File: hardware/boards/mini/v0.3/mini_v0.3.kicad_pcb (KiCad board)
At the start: 8 copper layers, 20 x 40 mm, 94 parts, among them IC1 NAU88C22YG, IC3 IS42S16160J-6BLI, J4 DF40C-90DP-0.4V, U2 LTV-217-G, U3 W25Q128JVS, U4 STM32H750XBHx, Y1 Crystal_GND24, Y3 32.768kHz

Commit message: mini: various final DFM tweaks
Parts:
- added G***: LOGO, LOGO, B.Cu at (72.4, 84.0)
- added kibuzzard-69637FF5: G***, kibuzzard-69637FF5, F.Cu at (71.5, 67.0)
- added kibuzzard-696388A5: G***, kibuzzard-696388A5, F.Cu at (88.5, 71.8)
- moved D2 4.51 mm to (85.0, 58.3)
- moved R15 4.51 mm to (82.8, 58.1)
- moved D3 0.15 mm to (79.6, 87.2)
- moved FB2 0.15 mm to (78.2, 88.2)
- moved FB3 0.15 mm to (81.5, 88.4)
- moved R6 0.15 mm to (88.5, 85.0)
- moved R7 0.15 mm to (78.2, 86.3)
- moved U2 0.15 mm to (85.0, 86.7)
- moved D4 0.13 mm to (75.5, 58.3)
- moved R17 0.07 mm to (73.5, 58.1)
- moved C26 0.06 mm to (84.5, 95.1)
- moved C27 0.06 mm to (83.6, 95.1)
- moved C20 0.05 mm to (86.3, 95.1)
- moved C21 0.05 mm to (85.4, 95.1)
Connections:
- U4 pad A12: unconnected-(U4D-PD4-PadA12) -> /LED_STATUS
- U4 pad A4: unconnected-(U4I-PI4-PadA4) -> /LED_STATUS2
- U4 pad E3: /LED_STATUS -> unconnected-(U4C-PC13-PadE3)
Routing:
- net /LED_STATUS2: track 0.00 -> 3.74 mm
- net +3.3V: track 54.9 -> 57.1 mm
- net /LED_STATUS: track 0.00 -> 2.22 mm
- net /SPKL: track 17.6 -> 19.6 mm, vias 1 -> 2
- net /SPKR: track 15.9 -> 16.1 mm, vias 1 -> 2
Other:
- outline, holes or cut-outs redrawn
- board text added: "Corners bites radius is 1.1mm for M2 mounting bolts."
- board text added: "DF40C-90DP-0.4V"
- board text added: "QSPI FLASH"
- board text added: "SDRAM"
- board text added: "White square is replaced with a 5x5mm QR code by JLC when configured in the order."

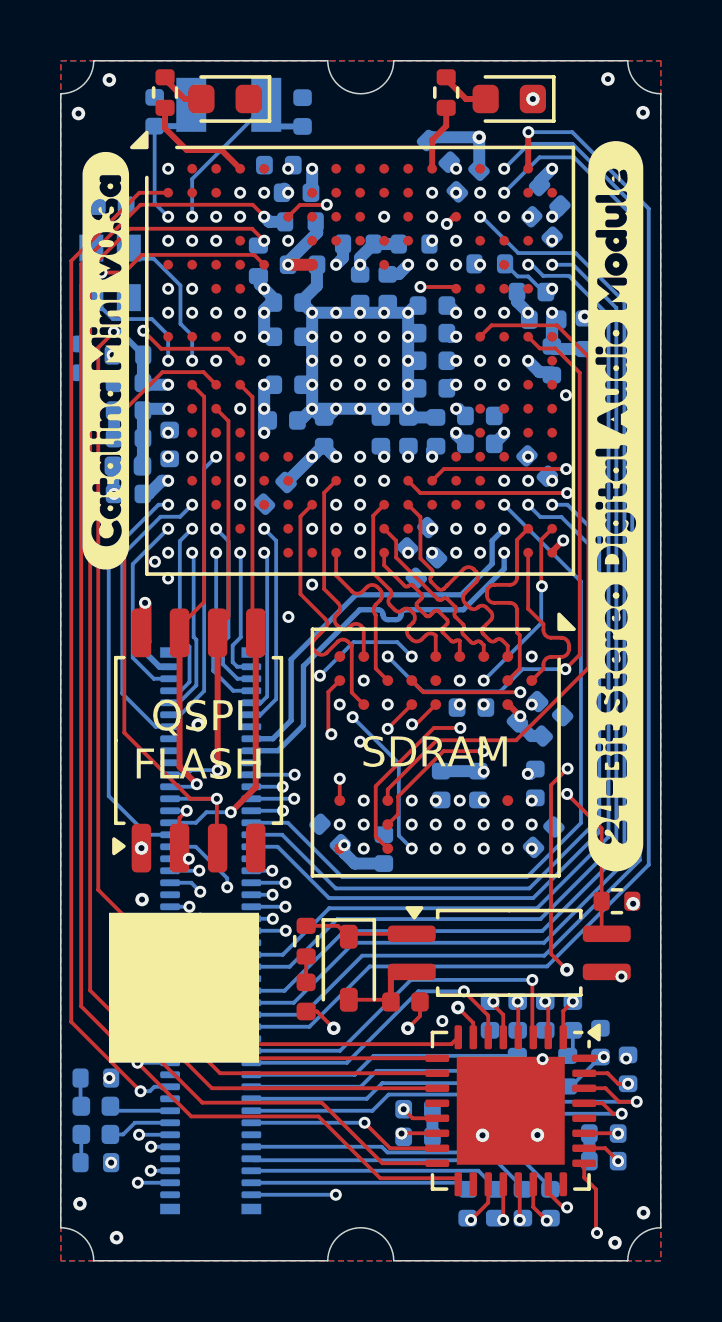
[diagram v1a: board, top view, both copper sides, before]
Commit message: mini: re-route status LED, add paws, expose copper on screw points
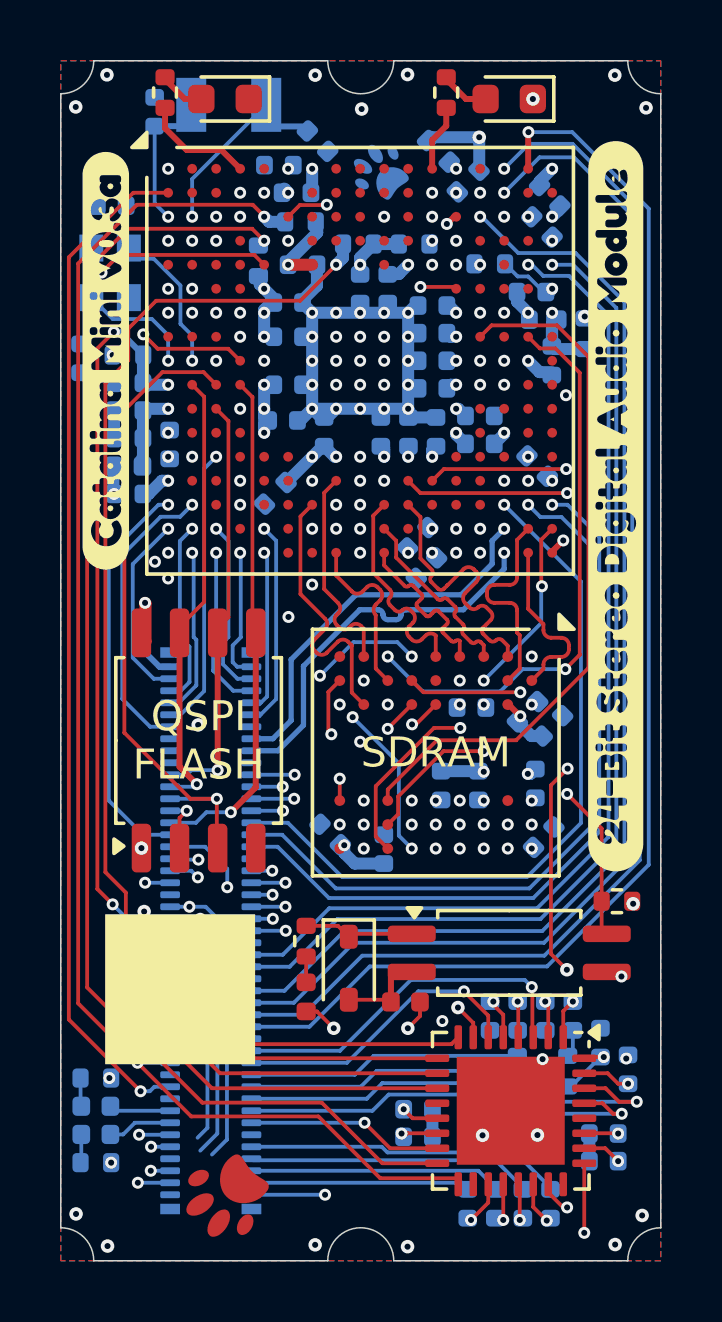
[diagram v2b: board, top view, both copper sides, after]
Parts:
- added G*** (x2): LOGO, LOGO, B.Cu at (80.7, 60.7)
- added J1: Conn_ARM_JTAG_SWD_10, Northernpaws:paw-3mm, F.Cu at (75.6, 94.8)
- moved C39 1.09 mm to (78.6, 59.7), turned to 135 degrees
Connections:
- J4 pad 29: /PC2_C -> /EXT_QSPI_DETECT
- R19 pad 2: /PC2_C -> /EXT_QSPI_DETECT
- U4 pad R1: /PC2_C -> /EXT_QSPI_DETECT
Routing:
- net /BOOT0: track 0.79 -> 31.2 mm, vias 1 -> 2
- net /EXT_QSPI_DETECT: track 0.00 -> 13.4 mm, vias 0 -> 1
- net /PC2_C: track 13.3 -> 0.00 mm, vias 1 -> 0
- net /SWD_IO: track 40.9 -> 50.1 mm
- net /SWD_CLK: track 43.0 -> 51.0 mm
- net /SWD_SWO: track 51.4 -> 58.6 mm
- net /PJ11: track 35.0 -> 36.7 mm
- net /SPKL: track 19.6 -> 19.0 mm
- net GND: vias 72 -> 77
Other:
- board text added: "For panels: JLC: 2 columns x 3 rows with edge rails"
- board text added: "northernpaws.io"
- board text removed: "@northernpaws"
